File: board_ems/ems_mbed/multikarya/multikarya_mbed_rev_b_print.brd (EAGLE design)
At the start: 87 x 107 mm, 156 parts, among them IC1 SIM900, IC2 74HC595D, IC3 74HC595D, IC4 ADE7758RW, J5 POWER_JACKPTH, U2 W5500

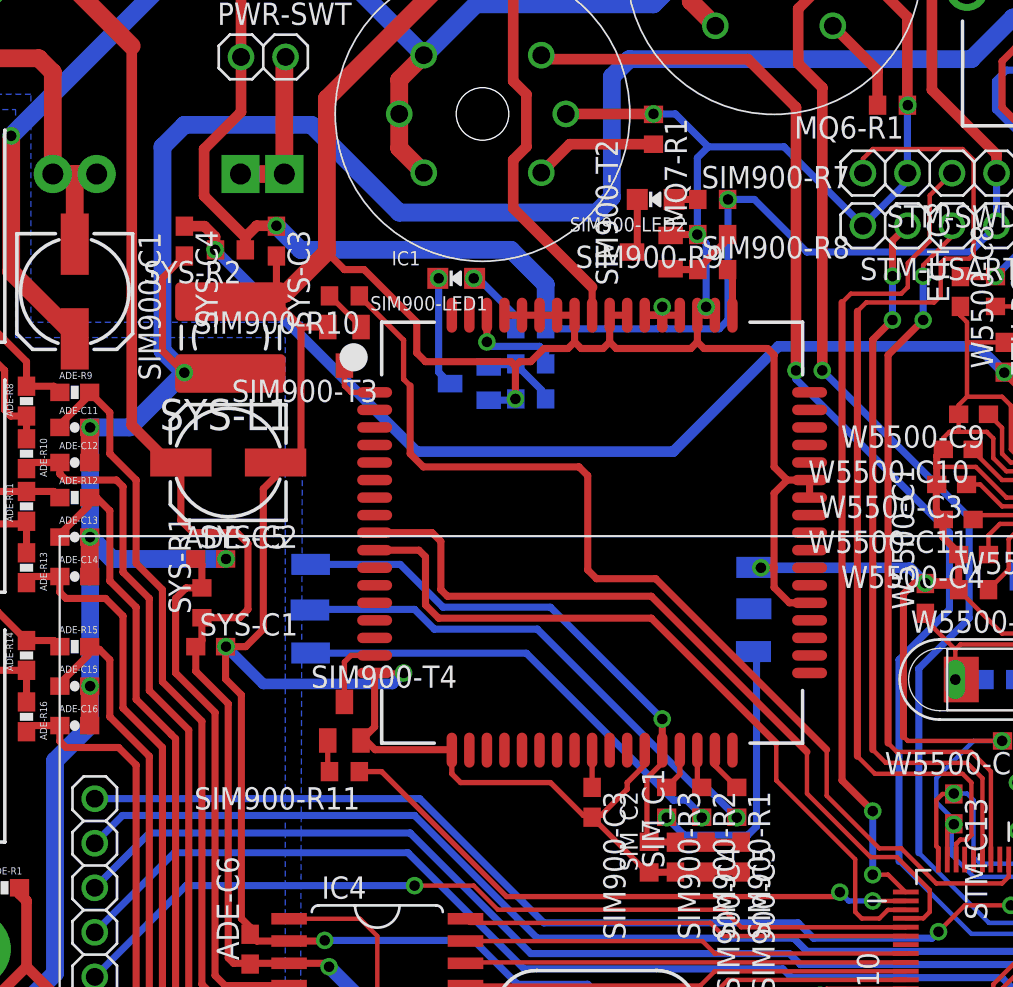
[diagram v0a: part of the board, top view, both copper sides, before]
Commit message: add doc for SLA
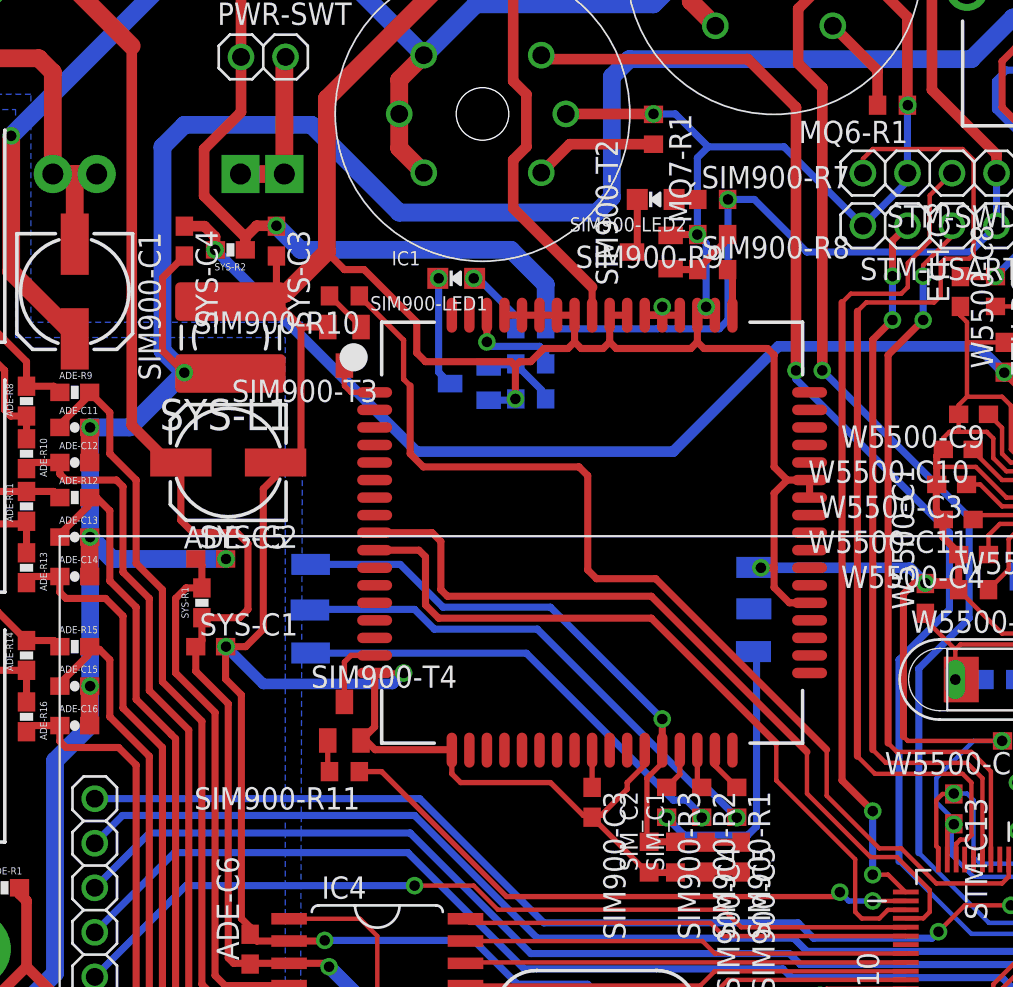
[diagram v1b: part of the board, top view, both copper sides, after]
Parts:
- ADE-C1, SYS-C1, SYS-C2, SYS-C3, SYS-C4: value 100nF -> 0.1uF
- DHT-R1, MQ6-R1, MQ7-R1: device rcl:R0603 -> resistor:R0603
- SIM_C1: device rcl:C0603 -> rcl:C0603K
- SYS-R1, SYS-R2: device rcl:R0603 -> SparkFun-Passives:0603-RES
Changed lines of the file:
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@@
 <element name="ADE-C14" library="SparkFun-Passives" package="0603-CAP" value="33nF" x="-71.5" y="63.5"/>
 <element name="ADE-C16" library="SparkFun-Passives" package="0603-CAP" value="33nF" x="-71.5" y="55"/>
-<element name="ADE-C1" library="rcl" package="C0603" value="100nF" x="-61.5" y="30.25" rot="R90"/>
+<element name="ADE-C1" library="rcl" package="C0603" value="0.1uF" x="-61.5" y="30.25" rot="R90"/>
 <element name="ADE-C2" library="rcl" package="C0805K" value="10uF" x="-63.5" y="30.25" rot="R90"/>
 <element name="ADE-C4" library="rcl" package="C0603" value="22pF" x="-43.25" y="36.75" rot="MR180"/>
@@
 <element name="SIM900-C4" library="rcl" package="C0603" value="100nF" x="-35.5" y="47.5" rot="R270"/>
 <element name="ETHERNET" library="microbuilder" package="RJ45_PULSEJACK" value="" x="-12.75" y="100"/>
-<element name="SIM_C1" library="rcl" package="C0603" value="100nF" x="-37.25" y="47.5" rot="R90"/>
+<element name="SIM_C1" library="rcl" package="C0603K" value="100nF" x="-37.25" y="47.5" rot="R90"/>
 <element name="SIM_C2" library="rcl" package="C0603K" value="22pF" x="-38.75" y="47.5" rot="R90"/>
 <element name="IC1" library="microbuilder" package="SIM900_SMT" value="SIM900" x="-42" y="66"/>
@@
 <element name="ADE-C6" library="rcl" package="C0603" value="100nF" x="-61.5" y="42.25" rot="R90"/>
 <element name="SYS-L1" library="rcl" package="POWER-CHOKE_WE-TPC" value="150Mhz" x="-62.625" y="77.125" rot="R180"/>
-<element name="SYS-R1" library="rcl" package="R0603" value="10R" x="-64.25" y="62" rot="R90"/>
-<element name="SYS-C1" library="rcl" package="C0603" value="100nF" x="-63.75" y="59.5"/>
-<element name="SYS-C2" library="rcl" package="C0603" value="100nF" x="-63.75" y="64.5"/>
+<element name="SYS-R1" library="SparkFun-Passives" package="0603-RES" value="10R" x="-64.25" y="62" rot="R90"/>
+<element name="SYS-C1" library="rcl" package="C0603" value="0.1uF" x="-63.75" y="59.5"/>
+<element name="SYS-C2" library="rcl" package="C0603" value="0.1uF" x="-63.75" y="64.5"/>
 <element name="W5500-C6" library="rcl" package="C0603" value="100nF" x="-10.25" y="76.75" rot="R90"/>
 <element name="W5500-C7" library="rcl" package="C0603" value="100nF" x="-13.875" y="76.75" rot="R90"/>
@@
 <element name="SIM900-R11" library="resistor" package="R0603" value="120R" x="-56.125" y="52.375" rot="R180"/>
 <element name="ESP-C1" library="rcl" package="C0603" value="100nF" x="-20.5" y="23.75"/>
-<element name="SYS-R2" library="rcl" package="R0603" value="10R" x="-62.625" y="82.125" rot="R180"/>
-<element name="SYS-C3" library="rcl" package="C0603" value="100nF" x="-60" y="82.625" rot="R270"/>
-<element name="SYS-C4" library="rcl" package="C0603" value="100nF" x="-65.25" y="82.625" rot="R270"/>
+<element name="SYS-R2" library="SparkFun-Passives" package="0603-RES" value="10R" x="-62.625" y="82.125" rot="R180"/>
+<element name="SYS-C3" library="rcl" package="C0603" value="0.1uF" x="-60" y="82.625" rot="R270"/>
+<element name="SYS-C4" library="rcl" package="C0603" value="0.1uF" x="-65.25" y="82.625" rot="R270"/>
 <element name="J5" library="SparkFun-Connectors" package="POWER_JACK_PTH" value="POWER_JACKPTH" x="-91" y="97.75" rot="R270">
 <attribute name="PROD_ID" value="CONN-08197" x="-91" y="97.75" size="1.778" layer="27" rot="R270" display="off"/>
@@
 <element name="SR_OUT1" library="pinhead" package="2X05/90" value="" x="-60.75" y="2" rot="R180"/>
 <element name="SR_OUT2" library="pinhead" package="2X05/90" value="" x="-39.875" y="2" rot="R180"/>
-<element name="DHT-R1" library="rcl" package="R0603" value="10k" x="-4.875" y="18" rot="MR90"/>
+<element name="DHT-R1" library="resistor" package="R0603" value="10k" x="-4.875" y="18" rot="MR90"/>
 <element name="SENSOR-MQ6" library="SparkFun-Sensors" package="MQ-3" value="METHANE_SENSOR" x="-31.625" y="98.25"/>
 <element name="SENSOR-MQ7" library="SparkFun-Sensors" package="MQ-3" value="METHANE_SENSOR" x="-48.25" y="89.875"/>
-<element name="MQ6-R1" library="rcl" package="R0603" value="10k" x="-24.875" y="90.375" rot="R180"/>
-<element name="MQ7-R1" library="rcl" package="R0603" value="10k" x="-38.5" y="89" rot="R270"/>
+<element name="MQ6-R1" library="resistor" package="R0603" value="10k" x="-24.875" y="90.375" rot="R180"/>
+<element name="MQ7-R1" library="resistor" package="R0603" value="10k" x="-38.5" y="89" rot="R270"/>
 <element name="U$4" library="TFT_LCD_2.2" package="TFT_LCD_2.2+F_CS" value="TFT_LCD_2.2+F_CS" x="-38.5" y="45.75"/>
 <element name="W5500-C12" library="rcl" package="153CLV-0605" value="10uF/16V" x="-4.875" y="85.25" rot="R180"/>
@@
 <wire x1="-19.125" y1="71.375" x2="-19.5" y2="71.75" width="0.254" layer="1"/>
 <wire x1="-21.975" y1="71.4" x2="-21.625" y2="71.75" width="0.254" layer="1"/>
-<wire x1="-37.225" y1="46.775" x2="-37.25" y2="46.65" width="0.4064" layer="1"/>
+<wire x1="-37.225" y1="46.775" x2="-37.25" y2="46.625" width="0.4064" layer="1"/>
 <wire x1="-39" y1="53.6" x2="-39" y2="52.75" width="0.3048" layer="1"/>
 <wire x1="-42" y1="49.775" x2="-42" y2="49.875" width="0.3048" layer="1"/>
@@
 <wire x1="-50.025" y1="53.625" x2="-50" y2="53.6" width="0.4064" layer="1"/>
 <wire x1="-33.5" y1="46.65" x2="-35.5" y2="46.65" width="0.4064" layer="1"/>
-<wire x1="-37.25" y1="46.65" x2="-35.525" y2="46.625" width="0.4064" layer="1"/>
+<wire x1="-37.25" y1="46.625" x2="-35.525" y2="46.625" width="0.4064" layer="1"/>
 <wire x1="-35.525" y1="46.625" x2="-35.5" y2="46.65" width="0.4064" layer="1"/>
-<wire x1="-38.75" y1="46.625" x2="-37.25" y2="46.65" width="0.4064" layer="1"/>
+<wire x1="-38.75" y1="46.625" x2="-37.25" y2="46.625" width="0.4064" layer="1"/>
 <wire x1="-38.975" y1="46.75" x2="-42" y2="49.775" width="0.3048" layer="1"/>
 <wire x1="-35.975" y1="83" x2="-36" y2="83" width="0.4064" layer="1"/>
@@
 <wire x1="-33.5" y1="48.35" x2="-35" y2="48.35" width="0.4064" layer="1"/>
 <wire x1="-35" y1="48.35" x2="-35.5" y2="48.35" width="0.4064" layer="1"/>
-<wire x1="-37.25" y1="48.35" x2="-35.025" y2="48.375" width="0.4064" layer="1"/>
+<wire x1="-37.25" y1="48.375" x2="-35.025" y2="48.375" width="0.4064" layer="1"/>
 <wire x1="-35.025" y1="48.375" x2="-35" y2="48.35" width="0.4064" layer="1"/>
-<wire x1="-38.75" y1="48.375" x2="-37.25" y2="48.35" width="0.4064" layer="1"/>
+<wire x1="-38.75" y1="48.375" x2="-37.25" y2="48.375" width="0.4064" layer="1"/>
 <wire x1="-38.875" y1="52" x2="-38.875" y2="48.5" width="0.3048" layer="1"/>
 <wire x1="-38.875" y1="48.5" x2="-38.75" y2="48.375" width="0.3048" layer="1"/>
